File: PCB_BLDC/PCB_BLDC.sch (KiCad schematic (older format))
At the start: 28 parts

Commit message: Main: Update Schematic Start PCB-Layout
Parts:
- removed C? (x2): C, symbol Device:C
- removed C?: C_Small, symbol Device:C_Small
- removed F?: Fuse, symbol Device:Fuse
- removed R?: R, symbol Device:R
- removed R? (x2): R_Small, symbol Device:R_Small
- added C1, C2: C_Small, symbol Device:C_Small
- added C10, C9: 1nF, symbol Device:C_Small
- added C12, C13, C21, C22: 100nF, symbol Device:C_Small
- added C16, C17, C18, C19: 220nF, symbol Device:C_Small
- added C24, C25: 470nF, symbol Device:C_Small
- added C3: 2200uF, symbol Device:C_Small
- added C6: 10nF, symbol Device:C_Small
- added D1: 12V, symbol Device:D_Zener_Small
- added Q1: IRF4905, Package_TO_SOT_SMD:TO-263-2_TabPin1, symbol Transistor_FET:IRF4905
- added R1, R5, R6: 1k, Resistor_SMD:R_1206_3216Metric_Pad1.30x1.75mm_HandSolder, symbol Device:R_Small
- added R10, R13: 0.51k, Resistor_SMD:R_1206_3216Metric_Pad1.30x1.75mm_HandSolder, symbol Device:R_Small
- added R11, R12, R14, R15: 10k, Resistor_SMD:R_1206_3216Metric_Pad1.30x1.75mm_HandSolder, symbol Device:R_Small
- added R2: 1M, Resistor_SMD:R_1206_3216Metric_Pad1.30x1.75mm_HandSolder, symbol Device:R_Small
- added R3: 2k, Resistor_SMD:R_1206_3216Metric_Pad1.30x1.75mm_HandSolder, symbol Device:R_Small
- added U3, U4: BTN8962TA, Package_TO_SOT_SMD:TO-263-7_TabPin4, symbol BTN8962TA:BTN8962TA
- C11: renamed from C?; value C_Small -> 100nF
- C14, C15: renamed from C?; value 220n -> 220nF
- C20: renamed from C?; value 100n -> 100nF
- C23: renamed from C?; value 470n -> 470nF
- C4: renamed from C?; value 0.33u -> 0.33uF
- C5: renamed from C?; value 0.1u -> 0.1uF
- C7: renamed from C?; value C_Small -> 10nF
- C8: renamed from C?; value C_Small -> 1nF
- R4: renamed from R?; value R_Small -> 1k; footprint (none) -> Resistor_SMD:R_1206_3216Metric_Pad1.30x1.75mm_HandSolder
- R7: renamed from R?; value R_Small -> 0.51k; footprint (none) -> Resistor_SMD:R_1206_3216Metric_Pad1.30x1.75mm_HandSolder
- R8, R9: renamed from R?; footprint (none) -> Resistor_SMD:R_1206_3216Metric_Pad1.30x1.75mm_HandSolder
- SW1: renamed from SW?; footprint (none) -> Rotary_Encoder:RotaryEncoder_Alps_EC12E-Switch_Vertical_H20mm
- U1: renamed from U?; footprint Package_TO_SOT_THT:TO-220-3_Vertical -> Package_TO_SOT_SMD:TO-263-2_TabPin1
- U2: renamed from U?; footprint (none) -> Package_TO_SOT_SMD:TO-263-7_TabPin4; symbol btn8962ta:BTN8962TA -> BTN8962TA:BTN8962TA
- gave numbers to parts that had none: 5
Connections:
- net labels added: L1_IN, L1_INH, L1_IS, L1_Sense, L2_IN, L2_INH, L2_IS, L2_Motor, L2_Sense, L3_IN, L3_INH, L3_IS, L3_Motor, L3_Sense, Pull_Up_Ard_A, Pull_Up_Ard_B, VCC_5V, VCC_Filtered
- net labels removed: Ard_Label, Arduino_VCC, Filtered_VCC, IO_Ard, PolaritySchematic
- wire segments 61 -> 163
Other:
- note added: "C 0.1uF - 0.01 uF\nFerrite Bead Impedance 50 to 100 ohm @ range of interest: 0.5 uH - 5 uH"
- moved on the sheet: C11, C14, C15, C20, C23, C4, C5, C7, C8, D3, L1, R4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

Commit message: Main: Improve Schematic
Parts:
- removed C4: 0.33uF, symbol Device:C_Small
- removed C5: 0.1uF, symbol Device:C_Small
- added C?: 10uF, symbol Device:C_Small
- added J?: Conn_01x01_Female, symbol Connector:Conn_01x01_Female
- added R? (x2): 10k, Resistor_SMD:R_1206_3216Metric_Pad1.30x1.75mm_HandSolder, symbol Device:R_Small
- C1, C2: value C_Small -> 10uF
- C6, C7: value 10nF -> 1uF
- D3: footprint (none) -> LED_SMD:LED_1206_3216Metric_Pad1.42x1.75mm_HandSolder
- L1: value L -> 22uH
- U1: value LF15_TO220 -> MagI3C WPMDH1100XX1S / 173010542; footprint Package_TO_SOT_SMD:TO-263-2_TabPin1 -> Package_SIP:SIP3_11.6x8.5mm
- U2, U3, U4: symbol BTN8962TA:BTN8962TA -> PCB_BLDC-rescue:BTN8962TA-BTN8962TA
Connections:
- net labels added: VCC_Polartiy_Check
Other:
- note added: "Collins-Filter\n"
- note added: "Reverse Polartiy Protection\n"
- moved on the sheet: A1, C1, C2, C3, C6, C7, D3, L1, R3, SW1, U1

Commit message: Main: Update Schematic
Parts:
- removed D2: D, symbol Device:D
- removed M1: Stepper_Motor_unipolar_6pin, symbol Motor:Stepper_Motor_unipolar_6pin
- added C5: 1500uF, Capacitor_SMD:CP_Elec_16x17.5, symbol Device:C_Small
- added D2: D_Schottky, Diode_SMD:D_SMB_Handsoldering, symbol Device:D_Schottky
- added J2, J3, J4, J5, J6, J7: Conn_01x01_Female, Connector_Pin:Pin_D1.0mm_L10.0mm, symbol Connector:Conn_01x01_Female
- added J8: VCC_Unregulated, Connector:Banana_Jack_1Pin, symbol Connector:Conn_01x01_Female
- added J9: VCC_GND, Connector:Banana_Jack_1Pin, symbol Connector:Conn_01x01_Female
- C1, C10, C11, C12, C13, C2, C6, C7, C8, C9: footprint (none) -> Capacitor_SMD:C_1206_3216Metric_Pad1.33x1.80mm_HandSolder
- C14, C15, C16, C17, C18, C19, C20, C21, C22, C23, C24, C25: footprint (none) -> Capacitor_SMD:C_Elec_5x5.4
- C3: value 2200uF -> 1500uF; footprint (none) -> Capacitor_SMD:CP_Elec_16x17.5
- C4: renamed from C?; footprint (none) -> Capacitor_SMD:C_1206_3216Metric_Pad1.33x1.80mm_HandSolder
- D1: footprint (none) -> Diode_SMD:D_SOD-123
- J1: renamed from J?; footprint (none) -> Connector_Pin:Pin_D1.0mm_L10.0mm
- L1: footprint (none) -> Inductor_SMD:L_1210_3225Metric_Pad1.42x2.65mm_HandSolder
- U2, U3, U4: symbol PCB_BLDC-rescue:BTN8962TA-BTN8962TA -> btn8962ta:BTN8962TA
- gave numbers to parts that had none: 2
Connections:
- wire segments 163 -> 176
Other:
- note added: "Elko notwendig\n"

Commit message: Main: Update Schmeatics and PCB
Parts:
- L1: footprint Inductor_SMD:L_1210_3225Metric_Pad1.42x2.65mm_HandSolder -> Inductor_SMD:L_Wuerth_WE-PD-Typ-LS_Handsoldering
- Q1: footprint Package_TO_SOT_SMD:TO-263-2_TabPin1 -> Package_TO_SOT_SMD:TO-263-2
- U2, U3, U4: footprint Package_TO_SOT_SMD:TO-263-7_TabPin4 -> Package_TO_SOT_SMD:TO-263-7_TabPin8
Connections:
- net Pull_Up_Ard_A is gone; now on net Rot_A_Pull_Up: R16.1, SW1.A
- net Pull_Up_Ard_B is gone; now on net Rot_B_Pull_Up: R17.1, SW1.B
- net VCC is gone; now on net VCC_Unregulated: Q1.2 (D)
- net GND: now also A1.29 (GND), A1.6 (GND), A1.7 (GND), C1.2, C15.2, C17.2, C19.2, C2.2, C20.2, C21.2, C22.2, C23.2, C24.2, C25.2, C3.2, C4.2, C5.2, U2.1, U3.1, U4.1
- net L1_IN: now also A1.17 (D2)
- net L1_INH: now also A1.20 (D5), R8.2
- net L1_IS: now also A1.23 (D8)
- net L1_Sense: now also A1.9 (A0)
- net L2_IN: now also A1.18 (D3)
- net L2_INH: now also A1.21 (D6), R11.2
- net L2_IS: now also A1.24 (D9)
- net L2_Sense: now also A1.10 (A1)
- net L3_IN: now also A1.19 (D4)
- net L3_INH: now also A1.22 (D7), R14.2
- net L3_IS: now also A1.25 (D10)
- net L3_Sense: now also A1.11 (A2)
- net VCC_5V: now also A1.8 (VIN)
- net VCC_Filtered: now also C2.1, C3.1, C5.1, L1.2
- net Rot_B_Pull_Up: now reaches A1.27 (D12)
- net Rot_A_Pull_Up: now reaches A1.28 (D13)
- net VCC_Unregulated: now reaches J8.1 (Pin_1)
- no-connect marks 0 -> 13
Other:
- note removed: "Elko notwendig\n"
- moved on the sheet: A1, C6, C7, D2, J1, J2, J3, J4, J5, J6, J7, R16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

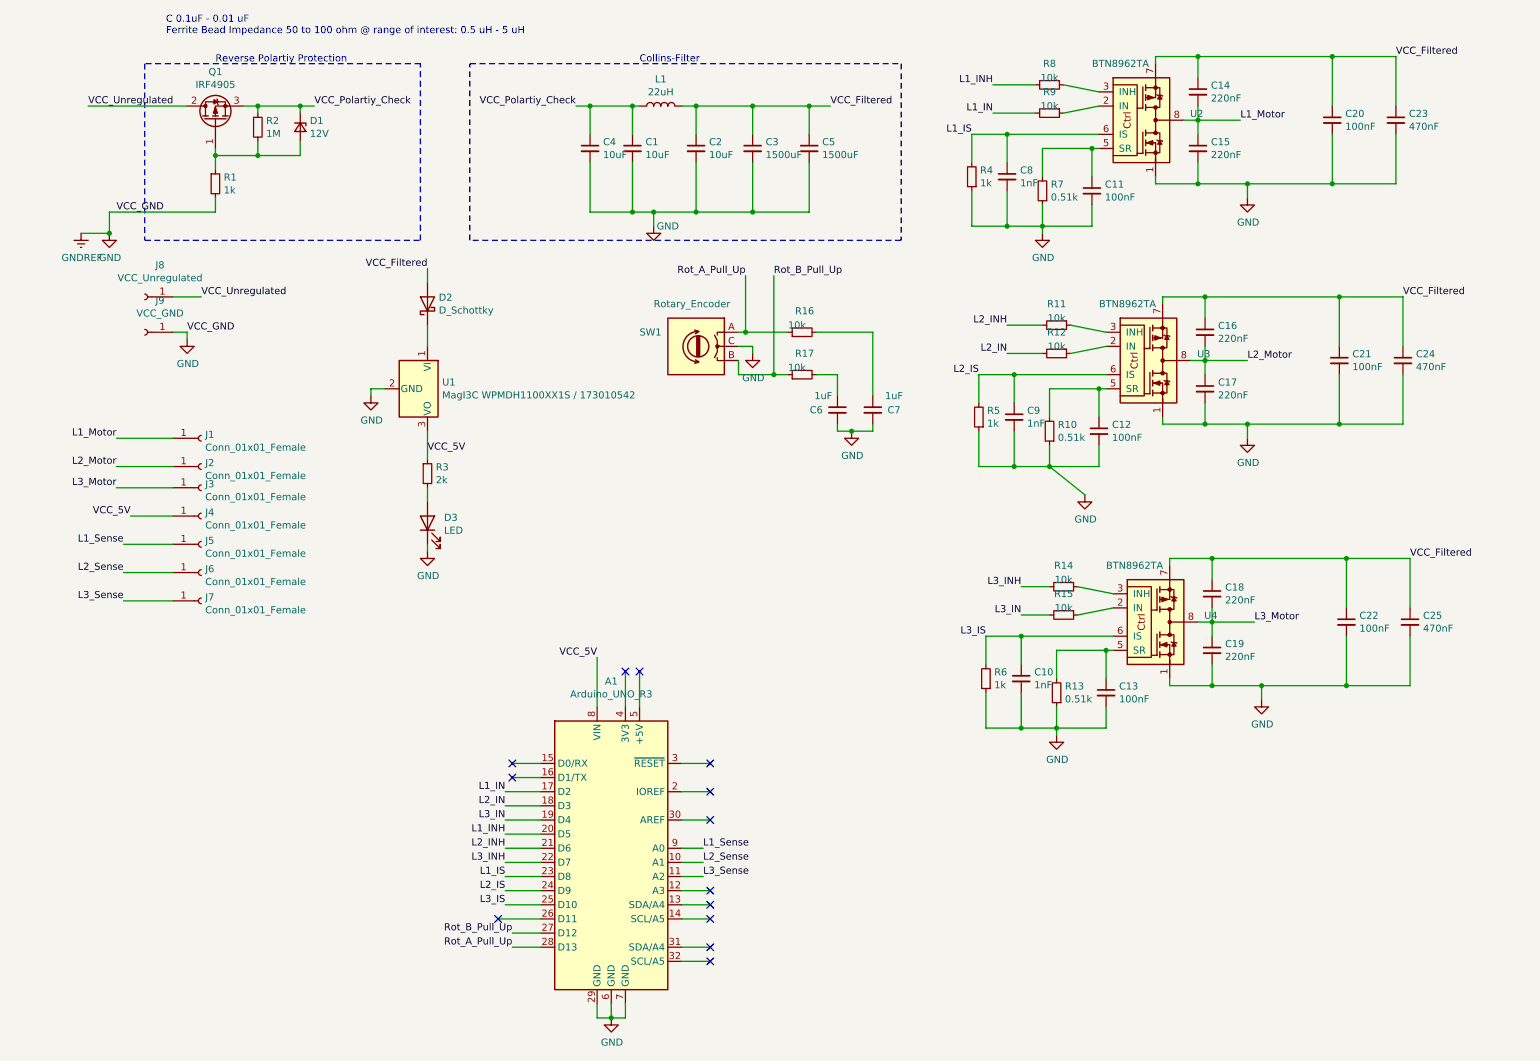
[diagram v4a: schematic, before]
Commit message: Main: Trace Routing @ PCB
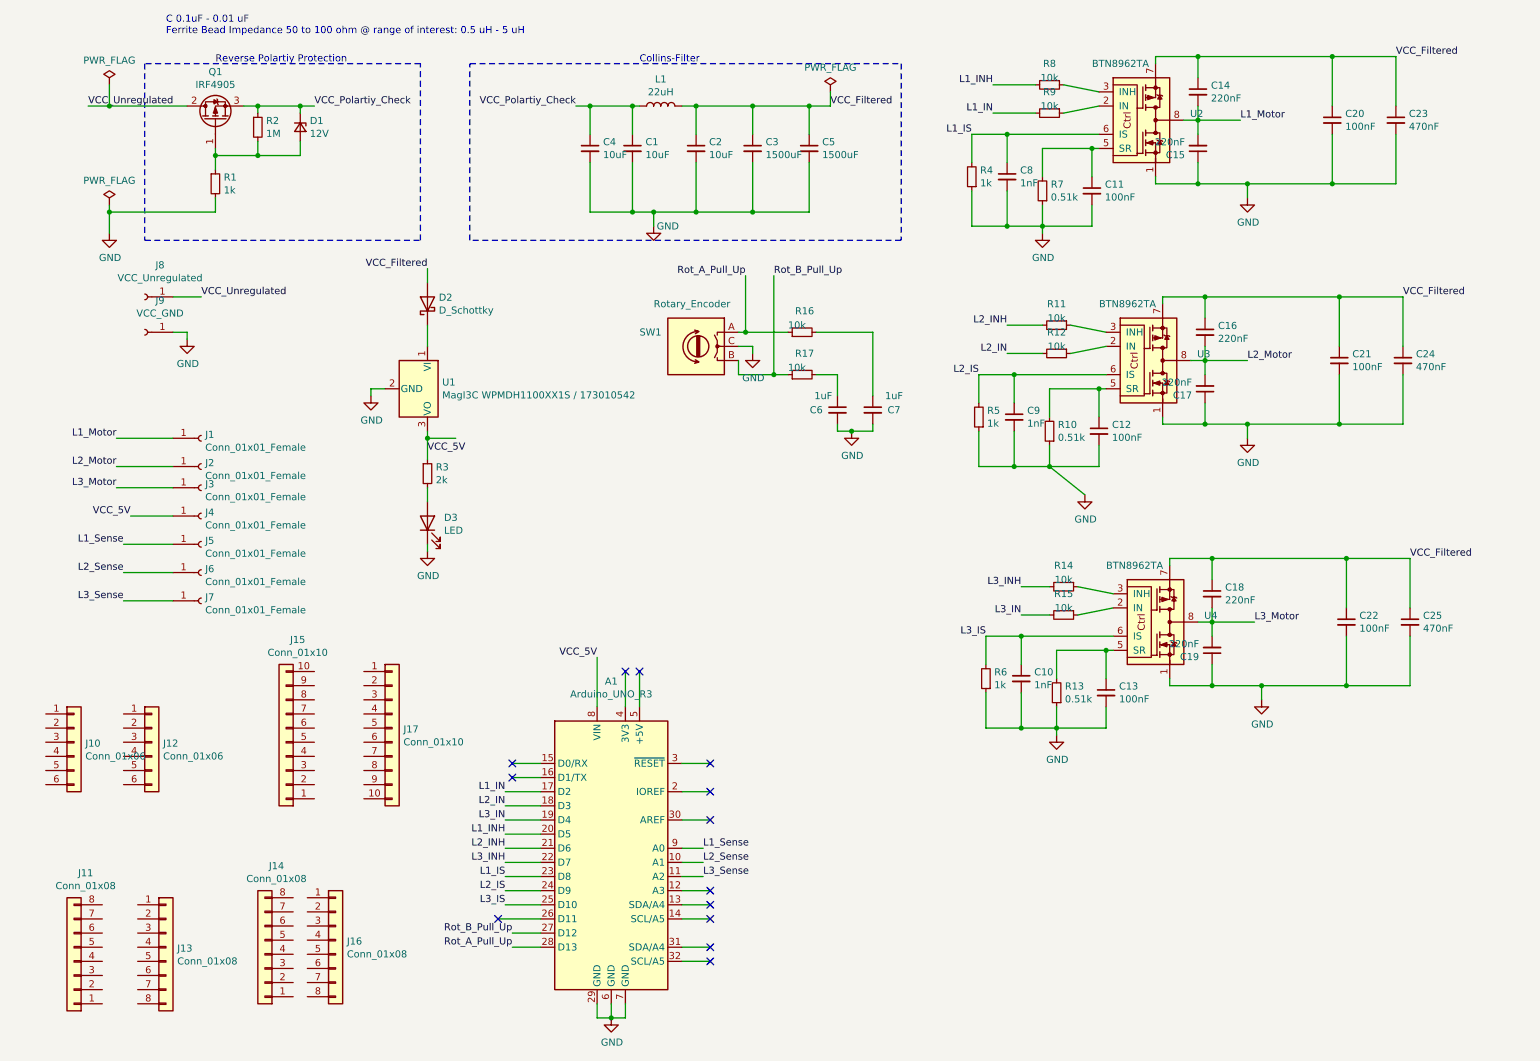
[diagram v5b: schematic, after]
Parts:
- added J10: Conn_01x06, Connector_PinHeader_2.54mm:PinHeader_1x06_P2.54mm_Vertical, symbol Connector_Generic:Conn_01x06
- added J11, J14: Conn_01x08, Connector_PinHeader_2.54mm:PinHeader_1x08_P2.54mm_Vertical, symbol Connector_Generic:Conn_01x08
- added J12: Conn_01x06, Connector_PinSocket_2.54mm:PinSocket_1x06_P2.54mm_Vertical, symbol Connector_Generic:Conn_01x06
- added J13, J16: Conn_01x08, Connector_PinSocket_2.54mm:PinSocket_1x08_P2.54mm_Vertical, symbol Connector_Generic:Conn_01x08
- added J15: Conn_01x10, Connector_PinHeader_2.54mm:PinHeader_1x10_P2.54mm_Vertical, symbol Connector_Generic:Conn_01x10
- added J17: Conn_01x10, Connector_PinSocket_2.54mm:PinSocket_1x10_P2.54mm_Vertical, symbol Connector_Generic:Conn_01x10
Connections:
- net GND: now also C15.1, C17.1, C19.1; no longer C15.2, C17.2, C19.2
- net L1_Motor: now also C15.2; no longer C15.1
- net L2_Motor: now also C17.2; no longer C17.1
- net L3_Motor: now also C19.2; no longer C19.1
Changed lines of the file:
@@
 F 3 "~" H 8550 1450 50  0001 C CNN
 	1    8550 1450
-	1    0    0    -1
+	-1   0    0    1
 $EndComp
 Wire Wire Line
@@
 F 3 "~" H 8600 3150 50  0001 C CNN
 	1    8600 3150
-	1    0    0    -1
+	-1   0    0    1
 $EndComp
 Wire Wire Line
@@
 F 3 "~" H 8650 5000 50  0001 C CNN
 	1    8650 5000
-	1    0    0    -1
+	-1   0    0    1
 $EndComp
 Wire Wire Line
@@
 	3400 850  6450 850
 Wire Wire Line
-	3100 3450 3100 3650
+	3100 3450 3100 3500
 $Comp
 L power:GND #PWR01
@@
 VCC_Unregulated
 Wire Wire Line
-	700  1150 1400 1150
+	700  1150 850  1150
 Wire Wire Line
 	4600 5150 4600 5400
-Text Label 1400 2750 0    50   ~ 0
-VCC_GND
-Text Label 900  1900 0    50   ~ 0
-VCC_GND
 $Comp
 L power:GND #PWR0104
@@
 Connection ~ 9550 2500
 $Comp
-L power:GNDREF #PWR0103
-U 1 1 61E4725E
-P 650 2050
-F 0 "#PWR0103" H 650 1800 50  0001 C CNN
-F 1 "GNDREF" H 655 1877 50  0000 C CNN
-F 2 "" H 650 2050 50  0001 C CNN
-F 3 "" H 650 2050 50  0001 C CNN
-	1    650  2050
-	1    0    0    -1
-$EndComp
-Wire Wire Line
-	650  2050 850  2050
-Wire Wire Line
-	850  2050 850  1900
-$Comp
 L power:GND #PWR0111
 U 1 1 61E58344
@@
 	1    0    0    -1
 $EndComp
-Connection ~ 850  2050
 $Comp
 L power:GND #PWR0109
@@
 Wire Wire Line
 	8300 2500 8300 2550
+$Comp
+L Connector_Generic:Conn_01x06 J12
+U 1 1 61804A99
+P 1150 5650
+F 0 "J12" H 1230 5642 50  0000 L CNN
+F 1 "Conn_01x06" H 1230 5551 50  0000 L CNN
+F 2 "Connector_PinSocket_2.54mm:PinSocket_1x06_P2.54mm_Vertical" H 1150 5650 50  0001 C CNN
+F 3 "~" H 1150 5650 50  0001 C CNN
+	1    1150 5650
+	1    0    0    -1
+$EndComp
+$Comp
+L Connector_Generic:Conn_01x08 J13
+U 1 1 61805D97
+P 1250 7100
+F 0 "J13" H 1330 7092 50  0000 L CNN
+F 1 "Conn_01x08" H 1330 7001 50  0000 L CNN
+F 2 "Connector_PinSocket_2.54mm:PinSocket_1x08_P2.54mm_Vertical" H 1250 7100 50  0001 C CNN
+F 3 "~" H 1250 7100 50  0001 C CNN
+	1    1250 7100
+	1    0    0    -1
+$EndComp
+$Comp
+L Connector_Generic:Conn_01x08 J16
+U 1 1 618081B3
+P 2450 7050
+F 0 "J16" H 2530 7042 50  0000 L CNN
+F 1 "Conn_01x08" H 2530 6951 50  0000 L CNN
+F 2 "Connector_PinSocket_2.54mm:PinSocket_1x08_P2.54mm_Vertical" H 2450 7050 50  0001 C CNN
+F 3 "~" H 2450 7050 50  0001 C CNN
+	1    2450 7050
+	1    0    0    -1
+$EndComp
+$Comp
+L Connector_Generic:Conn_01x06 J10
+U 1 1 61820A08
+P 600 5650
+F 0 "J10" H 680 5642 50  0000 L CNN
+F 1 "Conn_01x06" H 680 5551 50  0000 L CNN
+F 2 "Connector_PinHeader_2.54mm:PinHeader_1x06_P2.54mm_Vertical" H 600 5650 50  0001 C CNN
+F 3 "~" H 600 5650 50  0001 C CNN
+	1    600  5650
+	1    0    0    -1
+$EndComp
+$Comp
+L Connector_Generic:Conn_01x08 J14
+U 1 1 6182189C
+P 1950 7150
+F 0 "J14" H 1868 6525 50  0000 C CNN
+F 1 "Conn_01x08" H 1868 6616 50  0000 C CNN
+F 2 "Connector_PinHeader_2.54mm:PinHeader_1x08_P2.54mm_Vertical" H 1950 7150 50  0001 C CNN
+F 3 "~" H 1950 7150 50  0001 C CNN
+	1    1950 7150
+	-1   0    0    1
+$EndComp
+$Comp
+L Connector_Generic:Conn_01x08 J11
+U 1 1 61821F6F
+P 600 7200
+F 0 "J11" H 518 6575 50  0000 C CNN
+F 1 "Conn_01x08" H 518 6666 50  0000 C CNN
+F 2 "Connector_PinHeader_2.54mm:PinHeader_1x08_P2.54mm_Vertical" H 600 7200 50  0001 C CNN
+F 3 "~" H 600 7200 50  0001 C CNN
+	1    600  7200
+	-1   0    0    1
+$EndComp
+$Comp
+L Connector_Generic:Conn_01x10 J17
+U 1 1 617F9C89
+P 2850 5550
+F 0 "J17" H 2930 5542 50  0000 L CNN
+F 1 "Conn_01x10" H 2930 5451 50  0000 L CNN
+F 2 "Connector_PinSocket_2.54mm:PinSocket_1x10_P2.54mm_Vertical" H 2850 5550 50  0001 C CNN
+F 3 "~" H 2850 5550 50  0001 C CNN
+	1    2850 5550
+	1    0    0    -1
+$EndComp
+$Comp
+L Connector_Generic:Conn_01x10 J15
+U 1 1 617FA29A
+P 2100 5650
+F 0 "J15" H 2018 4925 50  0000 C CNN
+F 1 "Conn_01x10" H 2018 5016 50  0000 C CNN
+F 2 "Connector_PinHeader_2.54mm:PinHeader_1x10_P2.54mm_Vertical" H 2100 5650 50  0001 C CNN
+F 3 "~" H 2100 5650 50  0001 C CNN
+	1    2100 5650
+	-1   0    0    1
+$EndComp
+$Comp
+L power:PWR_FLAG #FLG0101
+U 1 1 61836C3D
+P 850 1000
+F 0 "#FLG0101" H 850 1075 50  0001 C CNN
+F 1 "PWR_FLAG" H 850 1173 50  0000 C CNN
+F 2 "" H 850 1000 50  0001 C CNN
+F 3 "~" H 850 1000 50  0001 C CNN
+	1    850  1000
+	1    0    0    -1
+$EndComp
+$Comp
+L power:PWR_FLAG #FLG0102
+U 1 1 61837D69
+P 850 1850
+F 0 "#FLG0102" H 850 1925 50  0001 C CNN
+F 1 "PWR_FLAG" H 850 2023 50  0000 C CNN
+F 2 "" H 850 1850 50  0001 C CNN
+F 3 "~" H 850 1850 50  0001 C CNN
+	1    850  1850
+	1    0    0    -1
+$EndComp
+Wire Wire Line
+	850  1850 850  1900
+Connection ~ 850  1900
+Wire Wire Line
+	850  1900 850  2050
+Wire Wire Line
+	850  1000 850  1150
+Connection ~ 850  1150
+Wire Wire Line
+	850  1150 1400 1150
+Wire Wire Line
+	3300 3500 3100 3500
+Connection ~ 3100 3500
+Wire Wire Line
+	3100 3500 3100 3650
+$Comp
+L power:PWR_FLAG #FLG0103
+U 1 1 618669A9
+P 5950 1050
+F 0 "#FLG0103" H 5950 1125 50  0001 C CNN
+F 1 "PWR_FLAG" H 5950 1223 50  0000 C CNN
+F 2 "" H 5950 1050 50  0001 C CNN
+F 3 "~" H 5950 1050 50  0001 C CNN
+	1    5950 1050
+	1    0    0    -1
+$EndComp
+Wire Wire Line
+	5950 1050 5950 1150
 $EndSCHEMATC

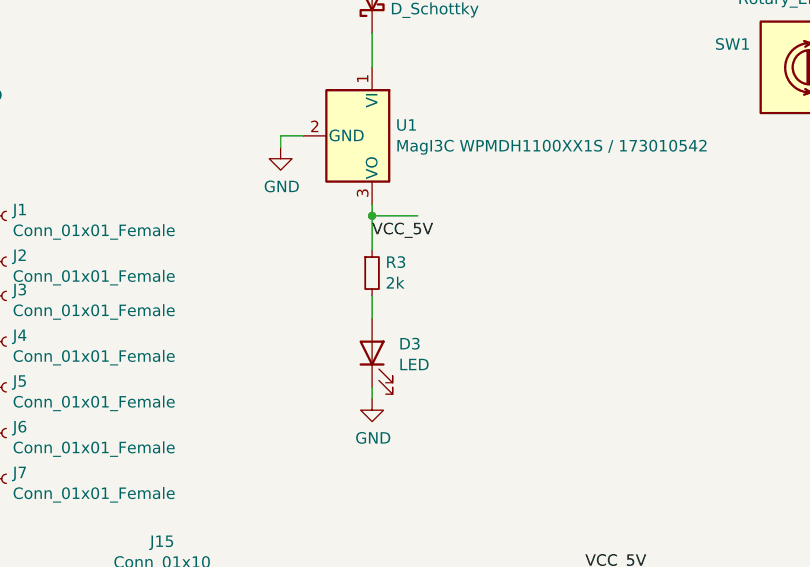
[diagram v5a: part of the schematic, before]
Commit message: Main: Update Footprint, PCB Layout
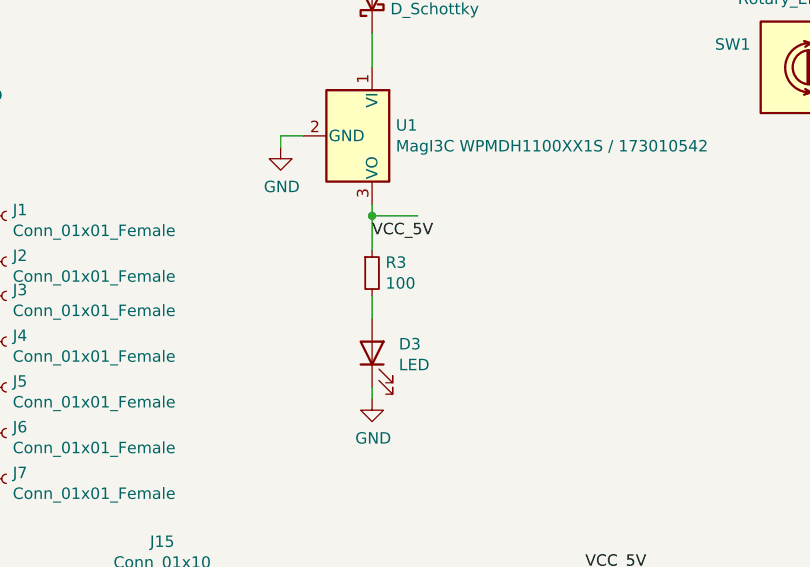
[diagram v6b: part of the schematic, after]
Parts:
- R3: value 2k -> 100
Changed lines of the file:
@@
 P 3100 3750
 F 0 "R3" H 3159 3796 50  0000 L CNN
-F 1 "2k" H 3159 3705 50  0000 L CNN
+F 1 "100" H 3159 3705 50  0000 L CNN
 F 2 "Resistor_SMD:R_1206_3216Metric_Pad1.30x1.75mm_HandSolder" H 3100 3750 50  0001 C CNN
 F 3 "~" H 3100 3750 50  0001 C CNN
